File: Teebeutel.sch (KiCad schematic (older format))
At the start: 28 parts, among them J1 RJ45_Shielded, J2 Conn_01x30_Female, U1 ESP32-WROOM-32, U2 TLV1117-33, U3 MCP73831-2-OT, U4 SDB628

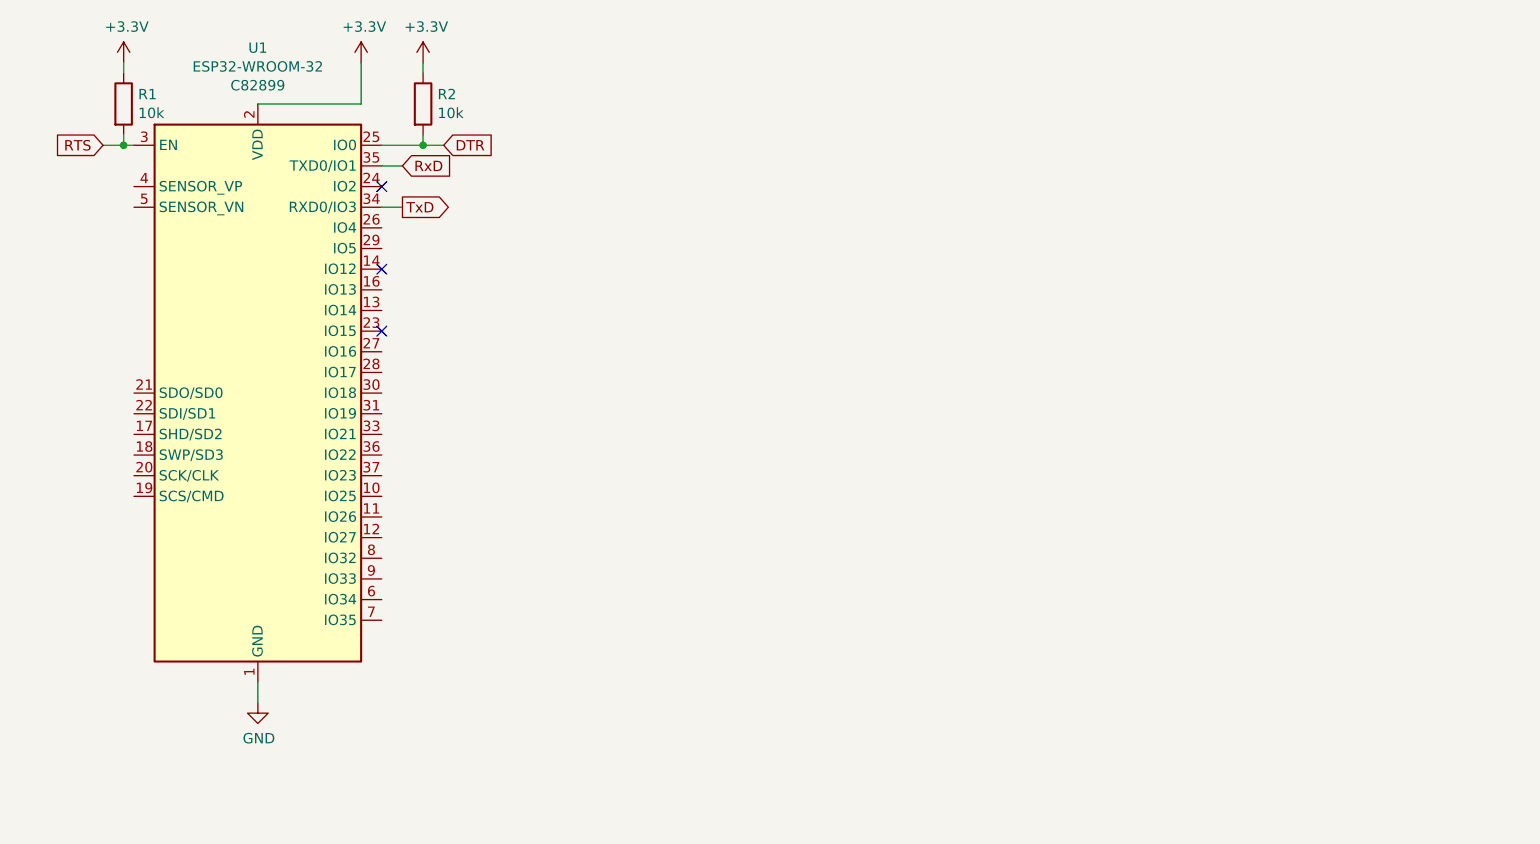
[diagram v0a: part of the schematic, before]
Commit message: feat: add SD-Card, accelerometer and SDI for display
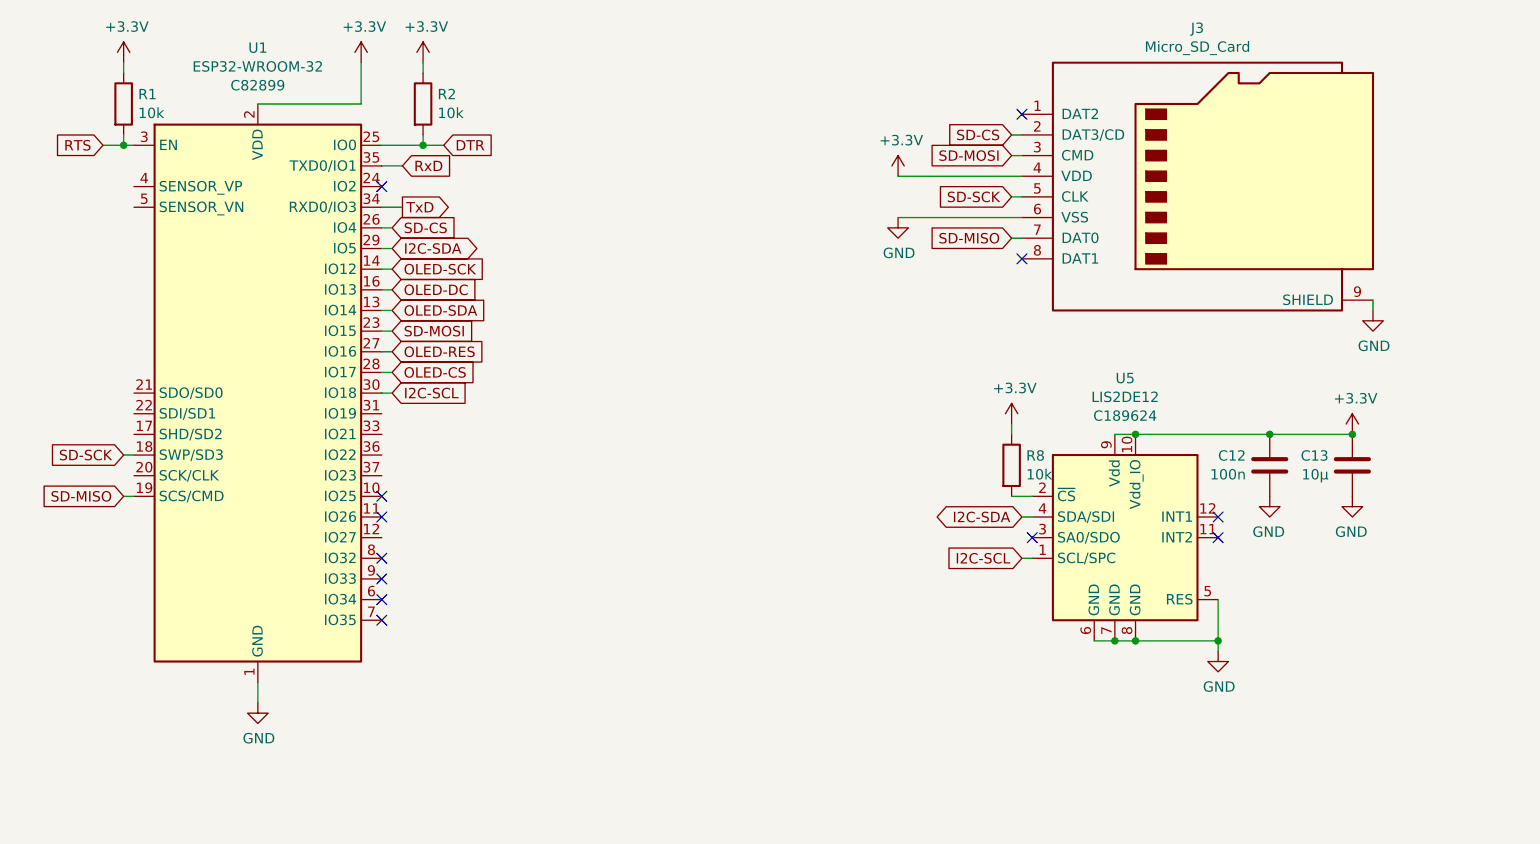
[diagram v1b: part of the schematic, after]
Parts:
- added C12: 100n, Capacitor_SMD:C_0603_1608Metric, symbol Device:C
- added C13: 10µ, Capacitor_SMD:C_0603_1608Metric, symbol Device:C
- added J3: Micro_SD_Card, Connector_Card:microSD_HC_Hirose_DM3AT-SF-PEJM5, symbol Connector:Micro_SD_Card
- added R8: 10k, Resistor_SMD:R_0603_1608Metric, symbol Device:R
- added U5: LIS2DE12, Package_LGA:LGA-12_2x2mm_P0.5mm, symbol Sensor_Motion:LIS2DE12
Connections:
- net +3V3: now also C12.1, C13.1, J3.4 (VDD), R8.1, U5.10 (Vdd_IO), U5.9 (Vdd)
- net GND: now also C12.2, C13.2, J3.6 (VSS), J3.9 (SHIELD), U5.5 (RES), U5.6 (GND), U5.7 (GND), U5.8 (GND)
- net OLED-CS: now also U1.28 (IO17)
- net OLED-DC: now also U1.16 (IO13)
- net OLED-RES: now also U1.27 (IO16)
- net OLED-SCK: now also U1.14 (IO12)
- net OLED-SDA: now also U1.13 (IO14)
- net SD-SCK: now reaches U1.18 (SWP/SD3)
- net SD-SCK: now also J3.5 (CLK)
- net SD-MISO: now reaches U1.19 (SCS/CMD)
- net SD-MISO: now also J3.7 (DAT0)
- net SD-MOSI: now reaches U1.23 (IO15)
- net SD-MOSI: now also J3.3 (CMD)
- net SD-CS: now reaches U1.26 (IO4)
- net SD-CS: now also J3.2 (DAT3/CD)
- net I2C-SDA: now reaches U1.29 (IO5)
- net I2C-SDA: now also U5.4 (SDA/SDI)
- net I2C-SCL: now reaches U1.30 (IO18)
- net I2C-SCL: now also U5.1 (SCL/SPC)
- new net: R8.2, U5.2 (~CS)
- no-connect marks 9 -> 18

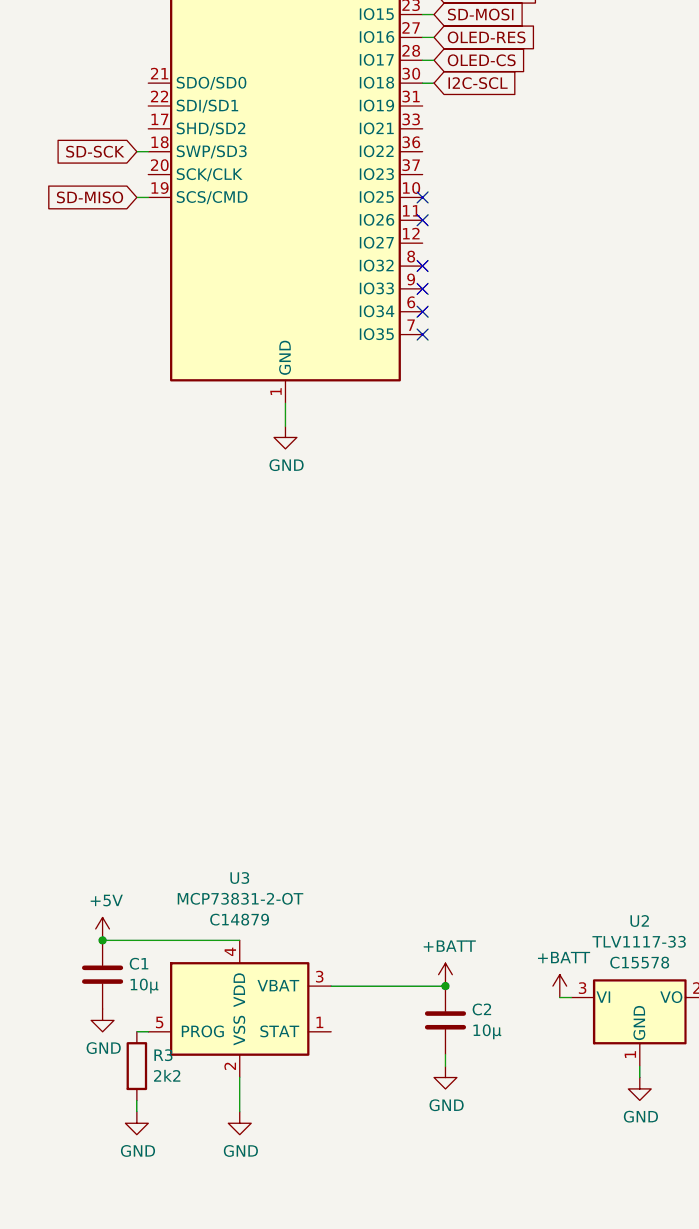
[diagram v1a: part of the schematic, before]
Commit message: feat: add chargin indicators and touch inputs
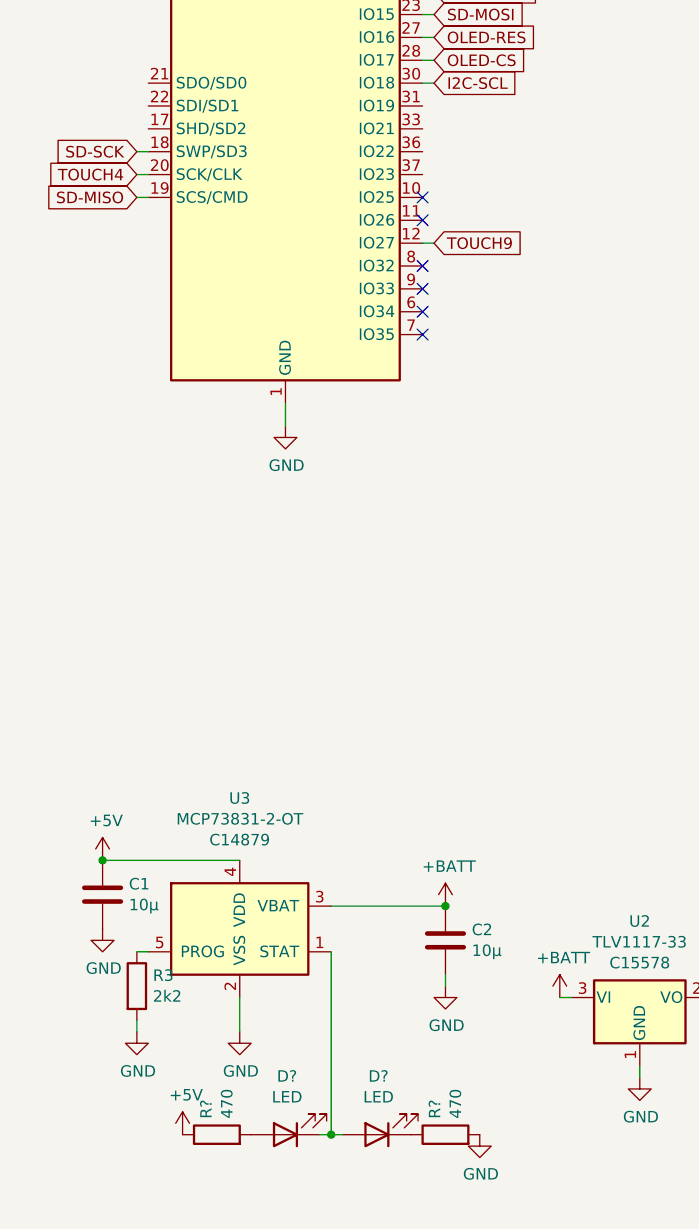
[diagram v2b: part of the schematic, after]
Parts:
- added D? (x2): LED, symbol Device:LED
- added R? (x2): 470, Resistor_SMD:R_0603_1608Metric, symbol Device:R
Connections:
- net +5V: now also R?.1
- net GND: now also R?.2
- net TOUCH9: now reaches U1.12 (IO27)
- net TOUCH4: now reaches U1.20 (SCK/CLK)
- net at U3.1 (STAT): now also D?.1 (K), D?.2 (A)
- new net: D?.2 (A), R?.2
- new net: D?.1 (K), R?.1
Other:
- moved on the sheet: C1, C2, R3, U3
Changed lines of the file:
@@
 L power:+BATT #PWR0112
 U 1 1 618B84B8
+P 2250 6250
+F 0 "#PWR0112" H 2250 6100 50  0001 C CNN
+F 1 "+BATT" H 2265 6423 50  0000 C CNN
+F 2 "" H 2250 6250 50  0001 C CNN
+F 3 "" H 2250 6250 50  0001 C CNN
+	1    2250 6250
+	1    0    0    -1
+$EndComp
+$Comp
+L power:GND #PWR0113
+U 1 1 618B8EAC
+P 1350 6800
+F 0 "#PWR0113" H 1350 6550 50  0001 C CNN
+F 1 "GND" H 1355 6627 50  0000 C CNN
+F 2 "" H 1350 6800 50  0001 C CNN
+F 3 "" H 1350 6800 50  0001 C CNN
+	1    1350 6800
+	1    0    0    -1
+$EndComp
+$Comp
+L Device:R R3
+U 1 1 618BD21B
+P 900 6600
+F 0 "R3" H 970 6646 50  0000 L CNN
+F 1 "2k2" H 970 6555 50  0000 L CNN
+F 2 "Resistor_SMD:R_0603_1608Metric" V 830 6600 50  0001 C CNN
+F 3 "~" H 900 6600 50  0001 C CNN
+	1    900  6600
+	1    0    0    -1
+$EndComp
+$Comp
+L power:GND #PWR0114
+U 1 1 618BDA3E
+P 900 6800
+F 0 "#PWR0114" H 900 6550 50  0001 C CNN
+F 1 "GND" H 905 6627 50  0000 C CNN
+F 2 "" H 900 6800 50  0001 C CNN
+F 3 "" H 900 6800 50  0001 C CNN
+	1    900  6800
+	1    0    0    -1
+$EndComp
+Wire Wire Line
+	1350 6650 1350 6800
+Wire Wire Line
+	900  6800 900  6750
+Wire Wire Line
+	950  6450 900  6450
+$Comp
+L power:+5V #PWR0115
+U 1 1 618C3DE7
+P 750 6050
+F 0 "#PWR0115" H 750 5900 50  0001 C CNN
+F 1 "+5V" H 765 6223 50  0000 C CNN
+F 2 "" H 750 6050 50  0001 C CNN
+F 3 "" H 750 6050 50  0001 C CNN
+	1    750  6050
+	1    0    0    -1
+$EndComp
+$Comp
+L Battery_Management:MCP73831-2-OT U3
+U 1 1 618B7477
+P 1350 6350
+F 0 "U3" H 1350 6921 50  0000 C CNN
+F 1 "MCP73831-2-OT" H 1350 6830 50  0000 C CNN
+F 2 "Package_TO_SOT_SMD:SOT-23-5" H 1400 6100 50  0001 L CIN
+F 3 "http://ww1.microchip.com/downloads/en/DeviceDoc/20001984g.pdf" H 1200 6300 50  0001 C CNN
+F 4 "C14879" H 1350 6739 50  0000 C CNN "JLCPCB"
+	1    1350 6350
+	1    0    0    -1
+$EndComp
+$Comp
+L Device:C C1
+U 1 1 618C8603
+P 750 6200
+F 0 "C1" H 865 6246 50  0000 L CNN
+F 1 "10µ" H 865 6155 50  0000 L CNN
+F 2 "Capacitor_SMD:C_0603_1608Metric" H 788 6050 50  0001 C CNN
+F 3 "~" H 750 6200 50  0001 C CNN
+	1    750  6200
+	1    0    0    -1
+$EndComp
+Connection ~ 750  6050
+$Comp
+L power:GND #PWR0116
+U 1 1 618C8D5D
+P 750 6350
+F 0 "#PWR0116" H 750 6100 50  0001 C CNN
+F 1 "GND" H 755 6177 50  0000 C CNN
+F 2 "" H 750 6350 50  0001 C CNN
+F 3 "" H 750 6350 50  0001 C CNN
+	1    750  6350
+	1    0    0    -1
+$EndComp
+$Comp
+L Device:C C2
+U 1 1 618C93C3
+P 2250 6400
+F 0 "C2" H 2365 6446 50  0000 L CNN
+F 1 "10µ" H 2365 6355 50  0000 L CNN
+F 2 "Capacitor_SMD:C_0603_1608Metric" H 2288 6250 50  0001 C CNN
+F 3 "~" H 2250 6400 50  0001 C CNN
+	1    2250 6400
+	1    0    0    -1
+$EndComp
+Wire Wire Line
+	750  6050 1350 6050
+$Comp
+L power:GND #PWR0117
+U 1 1 618CCD3C
 P 2250 6600
-F 0 "#PWR0112" H 2250 6450 50  0001 C CNN
-F 1 "+BATT" H 2265 6773 50  0000 C CNN
+F 0 "#PWR0117" H 2250 6350 50  0001 C CNN
+F 1 "GND" H 2255 6427 50  0000 C CNN
 F 2 "" H 2250 6600 50  0001 C CNN
 F 3 "" H 2250 6600 50  0001 C CNN
@@
 	1    0    0    -1
 $EndComp
-$Comp
-L power:GND #PWR0113
-U 1 1 618B8EAC
-P 1350 7150
-F 0 "#PWR0113" H 1350 6900 50  0001 C CNN
-F 1 "GND" H 1355 6977 50  0000 C CNN
-F 2 "" H 1350 7150 50  0001 C CNN
-F 3 "" H 1350 7150 50  0001 C CNN
-	1    1350 7150
-	1    0    0    -1
-$EndComp
-$Comp
-L Device:R R3
-U 1 1 618BD21B
-P 900 6950
-F 0 "R3" H 970 6996 50  0000 L CNN
-F 1 "2k2" H 970 6905 50  0000 L CNN
-F 2 "Resistor_SMD:R_0603_1608Metric" V 830 6950 50  0001 C CNN
-F 3 "~" H 900 6950 50  0001 C CNN
-	1    900  6950
-	1    0    0    -1
-$EndComp
-$Comp
-L power:GND #PWR0114
-U 1 1 618BDA3E
-P 900 7150
-F 0 "#PWR0114" H 900 6900 50  0001 C CNN
-F 1 "GND" H 905 6977 50  0000 C CNN
-F 2 "" H 900 7150 50  0001 C CNN
-F 3 "" H 900 7150 50  0001 C CNN
-	1    900  7150
-	1    0    0    -1
-$EndComp
-Wire Wire Line
-	1350 7000 1350 7150
-Wire Wire Line
-	900  7150 900  7100
-Wire Wire Line
-	950  6800 900  6800
-$Comp
-L power:+5V #PWR0115
-U 1 1 618C3DE7
-P 750 6400
-F 0 "#PWR0115" H 750 6250 50  0001 C CNN
-F 1 "+5V" H 765 6573 50  0000 C CNN
-F 2 "" H 750 6400 50  0001 C CNN
-F 3 "" H 750 6400 50  0001 C CNN
-	1    750  6400
-	1    0    0    -1
-$EndComp
-$Comp
-L Battery_Management:MCP73831-2-OT U3
-U 1 1 618B7477
-P 1350 6700
-F 0 "U3" H 1350 7271 50  0000 C CNN
-F 1 "MCP73831-2-OT" H 1350 7180 50  0000 C CNN
-F 2 "Package_TO_SOT_SMD:SOT-23-5" H 1400 6450 50  0001 L CIN
-F 3 "http://ww1.microchip.com/downloads/en/DeviceDoc/20001984g.pdf" H 1200 6650 50  0001 C CNN
-F 4 "C14879" H 1350 7089 50  0000 C CNN "JLCPCB"
-	1    1350 6700
-	1    0    0    -1
-$EndComp
-$Comp
-L Device:C C1
-U 1 1 618C8603
-P 750 6550
-F 0 "C1" H 865 6596 50  0000 L CNN
-F 1 "10µ" H 865 6505 50  0000 L CNN
-F 2 "Capacitor_SMD:C_0603_1608Metric" H 788 6400 50  0001 C CNN
-F 3 "~" H 750 6550 50  0001 C CNN
-	1    750  6550
-	1    0    0    -1
-$EndComp
-Connection ~ 750  6400
-$Comp
-L power:GND #PWR0116
-U 1 1 618C8D5D
-P 750 6700
-F 0 "#PWR0116" H 750 6450 50  0001 C CNN
-F 1 "GND" H 755 6527 50  0000 C CNN
-F 2 "" H 750 6700 50  0001 C CNN
-F 3 "" H 750 6700 50  0001 C CNN
-	1    750  6700
-	1    0    0    -1
-$EndComp
-$Comp
-L Device:C C2
-U 1 1 618C93C3
-P 2250 6750
-F 0 "C2" H 2365 6796 50  0000 L CNN
-F 1 "10µ" H 2365 6705 50  0000 L CNN
-F 2 "Capacitor_SMD:C_0603_1608Metric" H 2288 6600 50  0001 C CNN
-F 3 "~" H 2250 6750 50  0001 C CNN
-	1    2250 6750
-	1    0    0    -1
-$EndComp
-Wire Wire Line
-	750  6400 1350 6400
-$Comp
-L power:GND #PWR0117
-U 1 1 618CCD3C
-P 2250 6950
-F 0 "#PWR0117" H 2250 6700 50  0001 C CNN
-F 1 "GND" H 2255 6777 50  0000 C CNN
-F 2 "" H 2250 6950 50  0001 C CNN
-F 3 "" H 2250 6950 50  0001 C CNN
-	1    2250 6950
-	1    0    0    -1
-$EndComp
-Wire Wire Line
-	2250 6950 2250 6900
+Wire Wire Line
+	2250 6600 2250 6550
 Wire Wire Line
 	2050 1050 2050 1250
 Wire Wire Line
 	2050 1250 1550 1250
-Connection ~ 2250 6600
-Wire Wire Line
-	1750 6600 2250 6600
+Connection ~ 2250 6250
+Wire Wire Line
+	1750 6250 2250 6250
 $Comp
 L power:GND #PWR0118
@@
 Wire Wire Line
 	2200 2650 2150 2650
+Text GLabel 2200 3350 2    50   Input ~ 0
+TOUCH9
+Wire Wire Line
+	900  3050 950  3050
+Text GLabel 900  3050 0    50   Input ~ 0
+TOUCH4
+Wire Wire Line
+	2200 3350 2150 3350
+$Comp
+L Device:LED D?
+U 1 1 61954906
+P 1550 7250
+F 0 "D?" H 1543 6995 50  0000 C CNN
+F 1 "LED" H 1543 7086 50  0000 C CNN
+F 2 "" H 1550 7250 50  0001 C CNN
+F 3 "~" H 1550 7250 50  0001 C CNN
+	1    1550 7250
+	-1   0    0    1
+$EndComp
+$Comp
+L Device:LED D?
+U 1 1 619564E6
+P 1950 7250
+F 0 "D?" H 1943 6995 50  0000 C CNN
+F 1 "LED" H 1943 7086 50  0000 C CNN
+F 2 "" H 1950 7250 50  0001 C CNN
+F 3 "~" H 1950 7250 50  0001 C CNN
+	1    1950 7250
+	-1   0    0    1
+$EndComp
+$Comp
+L power:+5V #PWR?
+U 1 1 61959CF0
+P 1100 7250
+F 0 "#PWR?" H 1100 7100 50  0001 C CNN
+F 1 "+5V" H 1115 7423 50  0000 C CNN
+F 2 "" H 1100 7250 50  0001 C CNN
+F 3 "" H 1100 7250 50  0001 C CNN
+	1    1100 7250
+	1    0    0    -1
+$EndComp
+$Comp
+L Device:R R?
+U 1 1 6195B033
+P 1250 7250
+F 0 "R?" H 1320 7296 50  0000 L CNN
+F 1 "470" H 1320 7205 50  0000 L CNN
+F 2 "Resistor_SMD:R_0603_1608Metric" V 1180 7250 50  0001 C CNN
+F 3 "~" H 1250 7250 50  0001 C CNN
+	1    1250 7250
+	0    -1   -1   0
+$EndComp
+$Comp
+L Device:R R?
+U 1 1 6196DBD4
+P 2250 7250
+F 0 "R?" H 2320 7296 50  0000 L CNN
+F 1 "470" H 2320 7205 50  0000 L CNN
+F 2 "Resistor_SMD:R_0603_1608Metric" V 2180 7250 50  0001 C CNN
+F 3 "~" H 2250 7250 50  0001 C CNN
+	1    2250 7250
+	0    -1   -1   0
+$EndComp
+$Comp
+L power:GND #PWR?
+U 1 1 6196E12D
+P 2400 7250
+F 0 "#PWR?" H 2400 7000 50  0001 C CNN
+F 1 "GND" H 2405 7077 50  0000 C CNN
+F 2 "" H 2400 7250 50  0001 C CNN
+F 3 "" H 2400 7250 50  0001 C CNN
+	1    2400 7250
+	1    0    0    -1
+$EndComp
+Wire Wire Line
+	1750 6450 1750 7250
+Wire Wire Line
+	1750 7250 1800 7250
+Wire Wire Line
+	1700 7250 1750 7250
+Connection ~ 1750 7250
 $EndSCHEMATC
